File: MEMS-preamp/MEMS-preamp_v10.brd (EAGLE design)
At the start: 51 x 30 mm, 49 parts, among them IC1 BQ297X, IC2 OPA2134UA, IC3 MCP73831, IC4 SC4503, IC5 TPS7A49, IC6 QS6K1, J5 Battery, SW3 SPDT

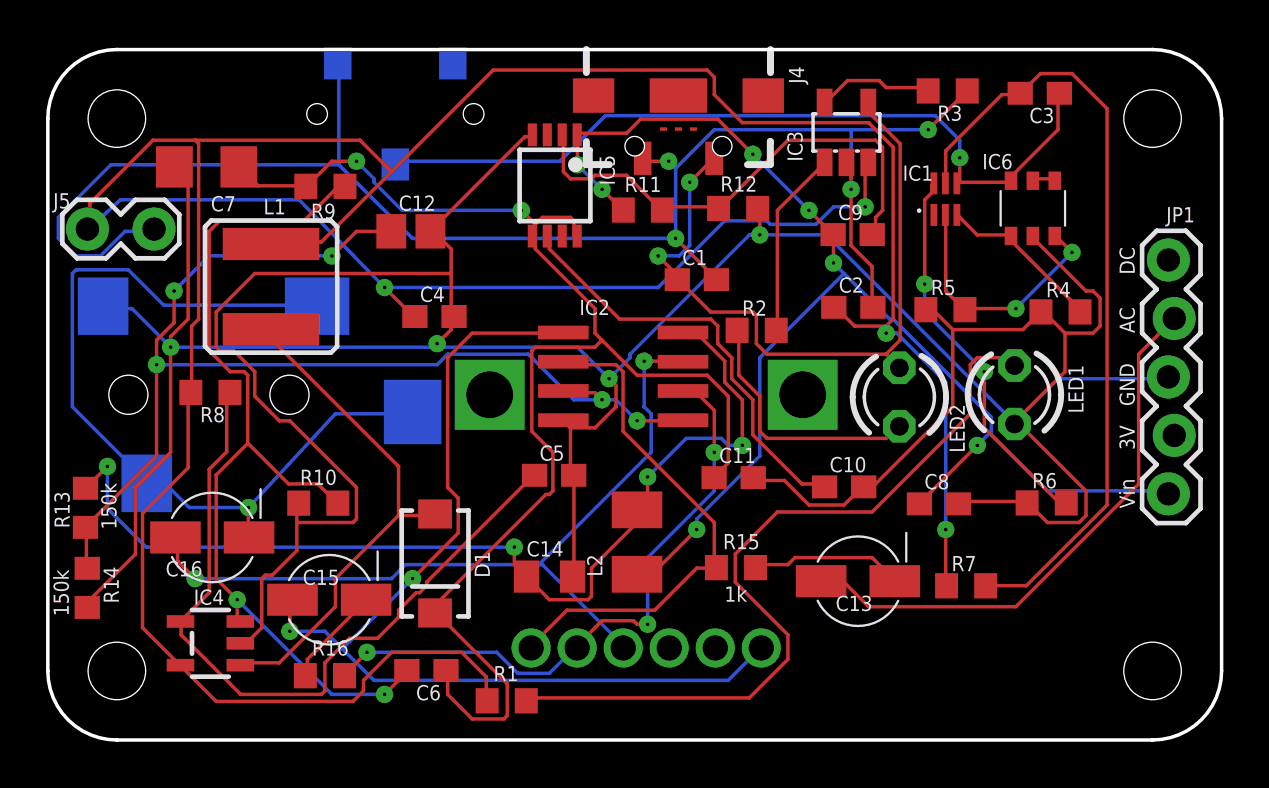
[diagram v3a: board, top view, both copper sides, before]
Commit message: drill sizes updated to 0.3mm (12mil)
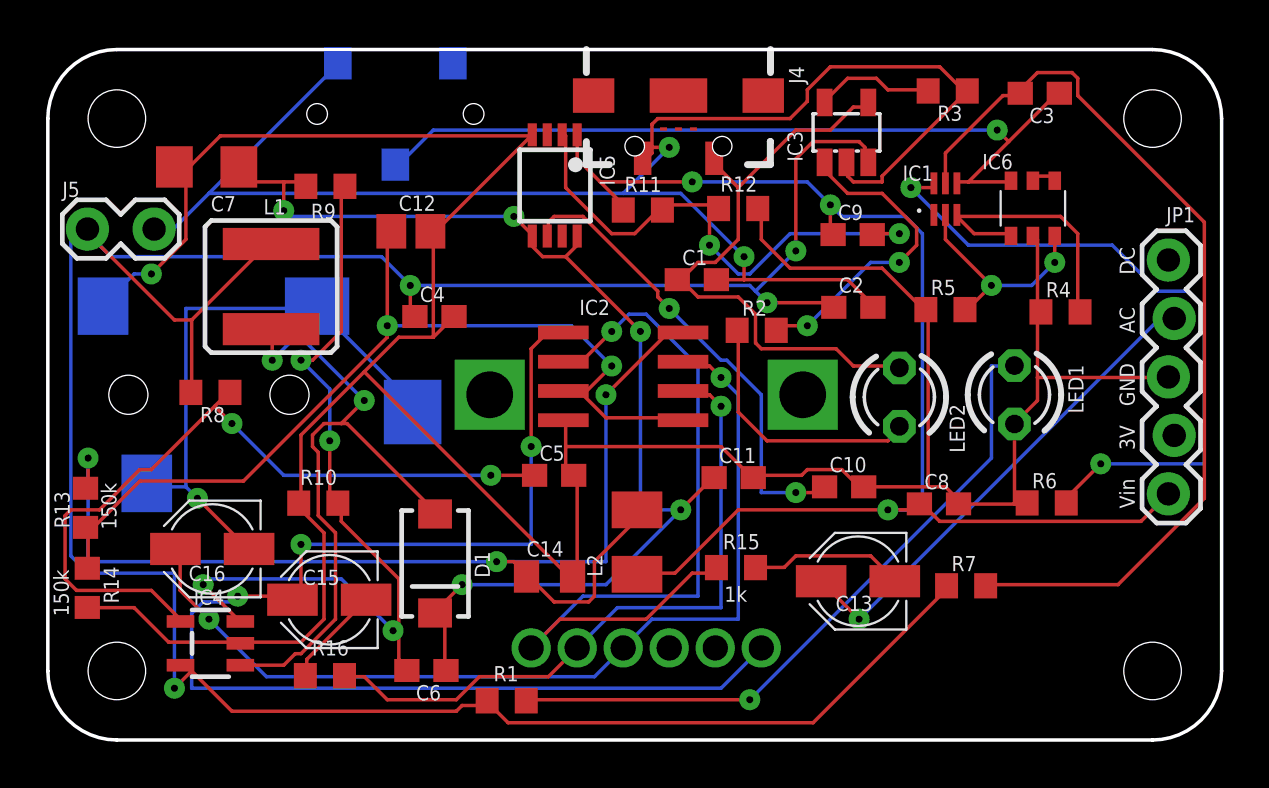
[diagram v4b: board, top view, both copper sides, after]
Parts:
- C13, C15, C16: device CMU-ArtFab:PANASONIC_B -> resistor:PANASONIC_B
- moved C16 0.50 mm to (7.14, 8.30)
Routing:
- net GND: track 177.8 -> 141.4 mm, vias 4 -> 1
- net VBAT: track 153.7 -> 123.7 mm
- net N$34: track 16.8 -> 29.7 mm
- net N$5: track 22.6 -> 35.4 mm, vias 0 -> 1
- net N$7: track 38.2 -> 25.4 mm
- net N$9: track 43.7 -> 56.2 mm, vias 2 -> 3
- net V+: track 61.3 -> 50.4 mm, vias 2 -> 5
- net N$8: track 50.3 -> 41.9 mm, vias 5 -> 2
- net N$12: track 22.3 -> 28.7 mm, vias 0 -> 2
- net N$10: track 35.2 -> 41.6 mm
- net N$15: track 43.8 -> 49.8 mm, vias 4 -> 3
- net N$42: track 34.4 -> 40.4 mm
- net N$25: track 8.17 -> 13.8 mm, vias 0 -> 2
- net N$2: track 34.7 -> 29.6 mm, vias 0 -> 1
- net N$27: track 7.32 -> 11.8 mm
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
